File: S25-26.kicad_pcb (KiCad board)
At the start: 6 copper layers, 90 x 90 mm, 198 parts, among them IC1 CMV4000-3E5M0PN, IC10 DS90LV048ATM_NOPB, IC11 DP83867IRPAPT, IC3 TPS5430DDAR, IC4 MT29F2G01ABAGDWB-IT_G_TR, IC5 MT29F2G01ABAGDWB-IT_G_TR, IC6 XMC7200D-E272K8384AA, IC7 DS90LV011AHMF_NOPB, IC8 DS90LV048ATM_NOPB, IC9 DS90LV048ATM_NOPB, J1 DC_IN_PADS, J2 Conn_01x06_Pin, J3 Conn_01x04_Pin, J4 RJ45_JXD1-0001NL, J5 Conn_01x04_Pin, Q1 ZXT849K, U1 TPS73601MDBVREP, U2 TPS73601MDBVREP, U3 TLS208D1EJVXUMA1, U4 TLS208D1EJVXUMA1, Y1 DSC1101DM2-012.0000, Y2 DSC1101DM2-125.0000T, Y3 DSC1101DM2-025.0000

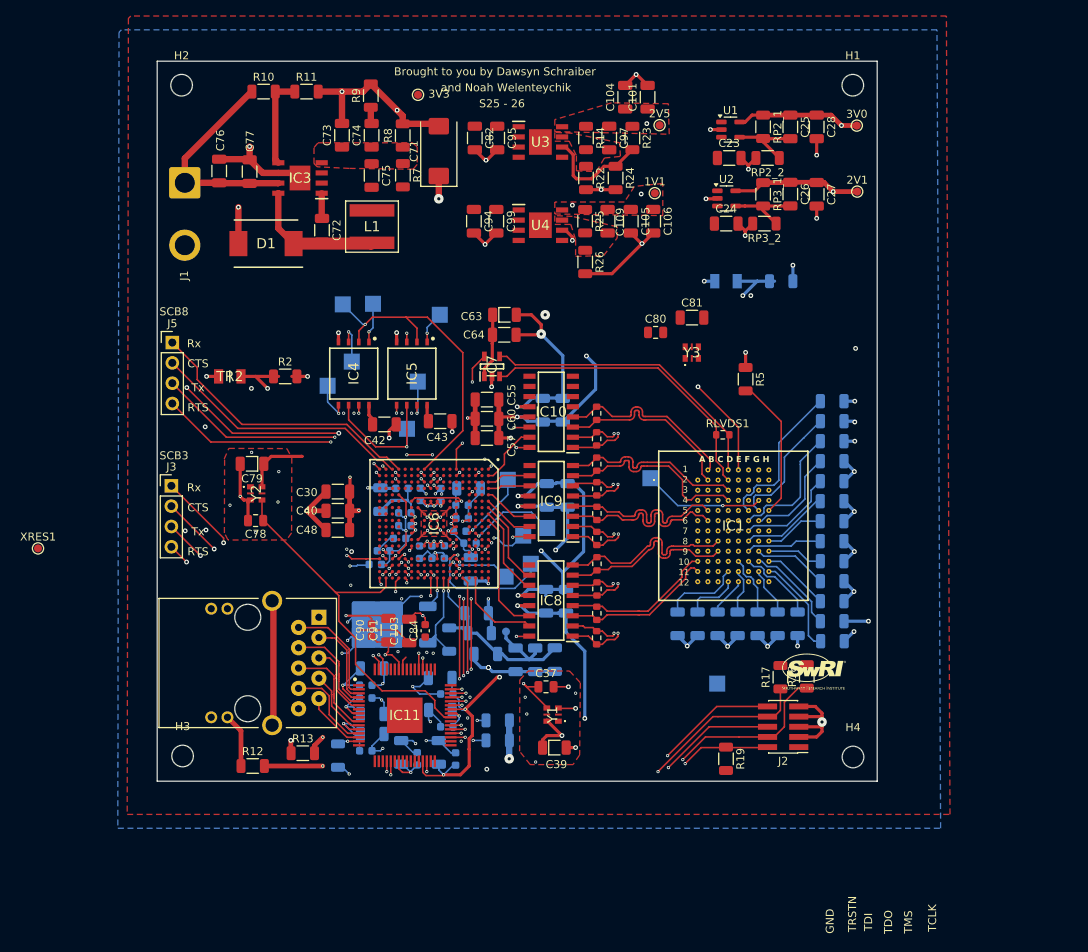
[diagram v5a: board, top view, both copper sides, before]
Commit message: V3 Almost Final
Move LVDS driver/change part if decided
Add thermal vias to GND pads of LDOs and ETH PHY.
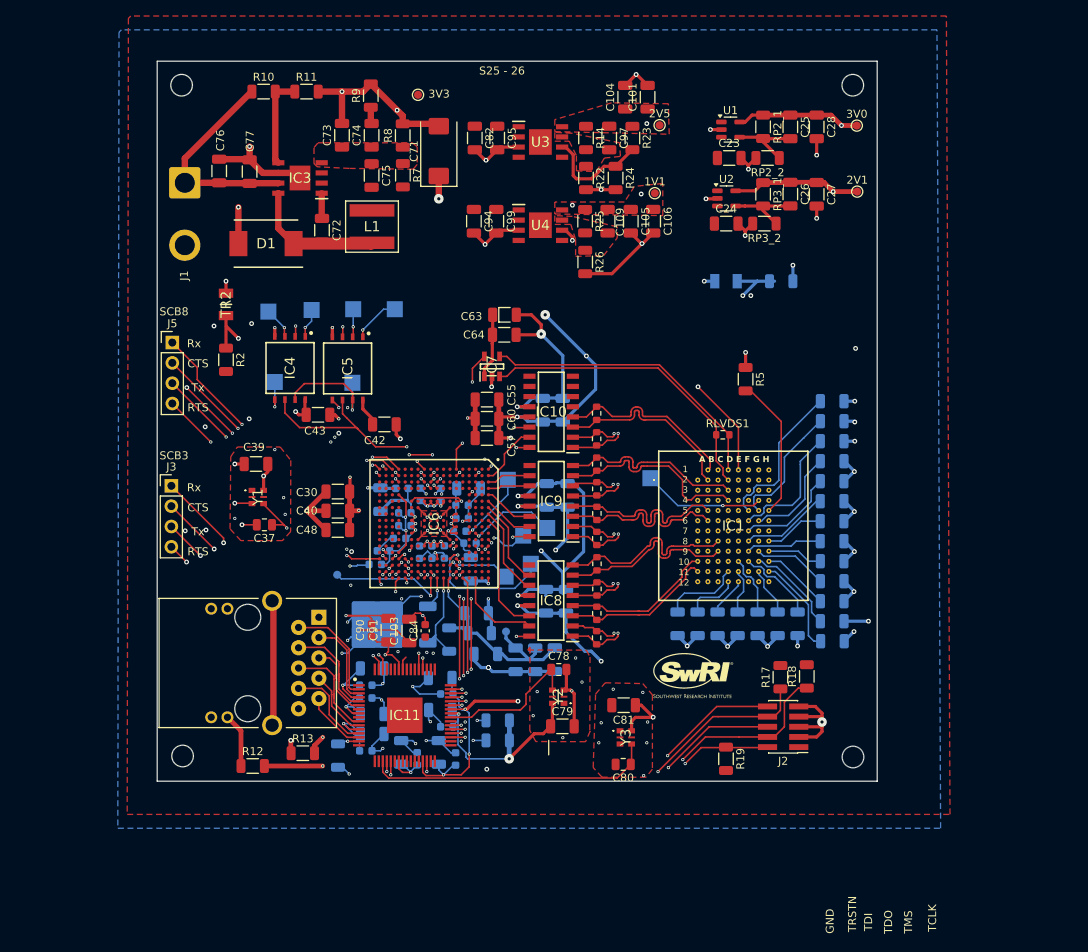
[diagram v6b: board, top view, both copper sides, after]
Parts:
- removed DRV_VOUT1: DRV_VOUT1, TestPoint:TestPoint_Pad_2.0x2.0mm
- removed the G*** at (190.5, 126.5)
- removed QSPI_SCLK1: QSPI_SCLK, TestPoint:TestPoint_Pad_2.0x2.0mm
- added G***: LOGO, SamacSys_Parts:logo, F.Cu at (175.4, 127.0)
- XRES1: moved to B.Cu
- moved C80 54.2 mm to (166.7, 138.1), turned to 180 degrees
- moved C39 51.5 mm to (120.8, 100.5), turned to 180 degrees
- moved C79 50.8 mm to (159.1, 133.3), turned to 0 degrees
- moved C81 49.2 mm to (166.7, 130.7), turned to 180 degrees
- moved Y3 48.8 mm to (167.0, 134.7), turned to -90 degrees
- moved Y1 45.8 mm to (121.0, 104.7), turned to -90 degrees
- moved Y2 45.5 mm to (158.5, 129.6), turned to 90 degrees
- moved C78 42.2 mm to (158.6, 126.2), turned to 0 degrees
- moved C37 40.6 mm to (121.8, 108.2), turned to 180 degrees
- moved XRES1 37.5 mm to (130.9, 114.4), turned to 180 degrees
- moved C43 15.3 mm to (128.5, 94.4)
- moved QSPI_IO2 12.2 mm to (122.3, 81.5), turned to 180 degrees
- moved TR2 9.01 mm to (117.0, 80.6), turned to 90 degrees
- moved QSPI_IO3 8.18 mm to (132.8, 90.4), turned to 180 degrees
- moved IC5 8.06 mm to (132.2, 88.6)
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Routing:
- net /Processing/XTAL_IN: track 0.00 -> 36.0 mm
- net /Processing/ETH0_REF_CLK (P18.0): track 48.4 -> 18.2 mm
- net GND: track 405.8 -> 383.4 mm, vias 100 -> 105
- net /Processing/HRSTN: track 19.6 -> 0.01 mm, vias 2 -> 0
- net +3V3: track 314.3 -> 296.6 mm, vias 39 -> 42
- net /Processing/XRES: track 57.1 -> 69.9 mm
- net /Processing/TEMPR_ADC1 (P6.1): track 26.9 -> 36.0 mm
- net /Processing/QSPI_IO1: track 41.0 -> 34.4 mm, vias 1 -> 3
- net /Processing/QSPI_SEL1: track 23.6 -> 29.2 mm
- net /Processing/QSPI_SCLK: track 25.0 -> 30.2 mm
- net /Processing/QSPI_IO2: track 35.3 -> 38.4 mm
- net /Processing/QSPI_IO0: track 35.5 -> 32.6 mm
- net +1V1: track 199.5 -> 196.8 mm, vias 8 -> 9
- net /Processing/QSPI_SEL0: track 26.5 -> 29.0 mm
- net /Processing/QSPI_IO3: track 25.7 -> 27.4 mm, vias 3 -> 2
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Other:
- board text removed: "Brought to you by Dawsyn Schraiber"
- board text removed: "and Noah Welenteychik"
